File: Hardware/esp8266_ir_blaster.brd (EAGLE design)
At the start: 25.9 x 32.6 mm, 54 parts, among them Q1 600mA/40V, U1 ESP-12S, U2 38kHz, U3 3.3V

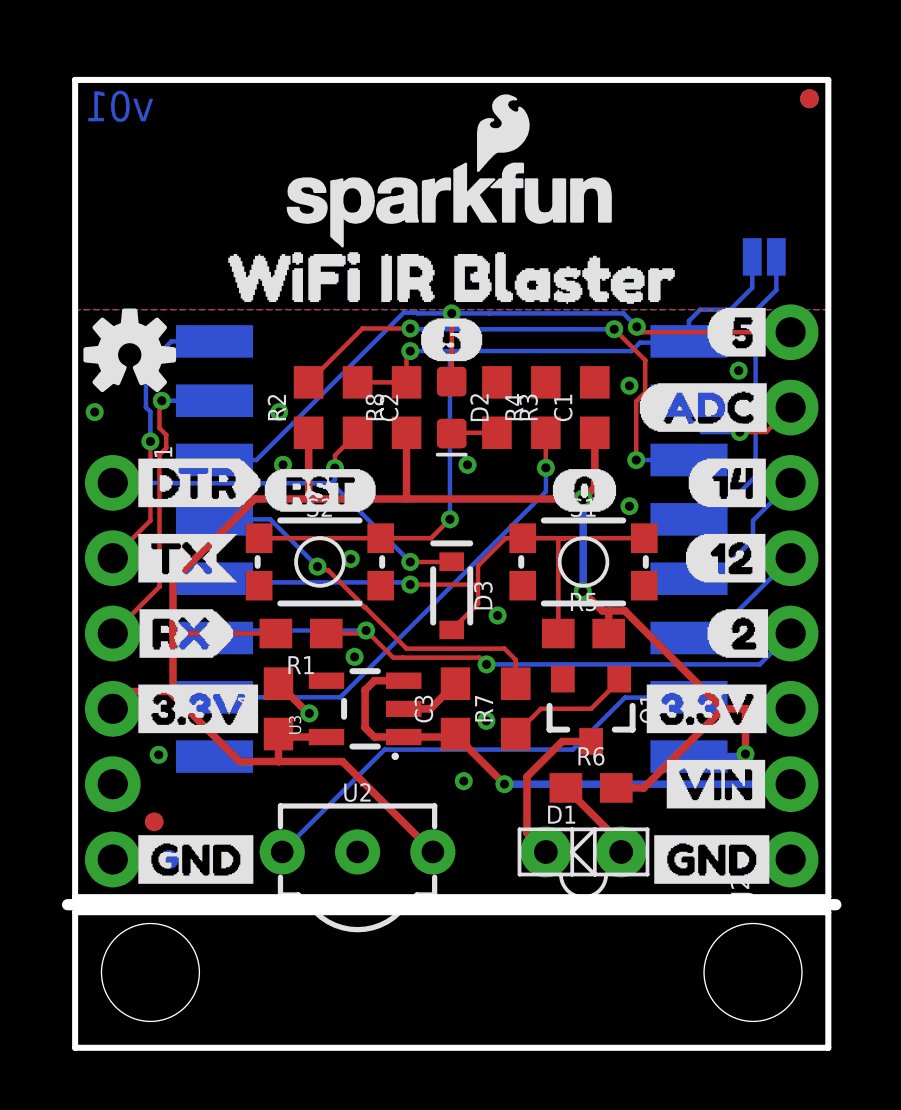
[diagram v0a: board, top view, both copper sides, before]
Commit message: Adding thermal pad
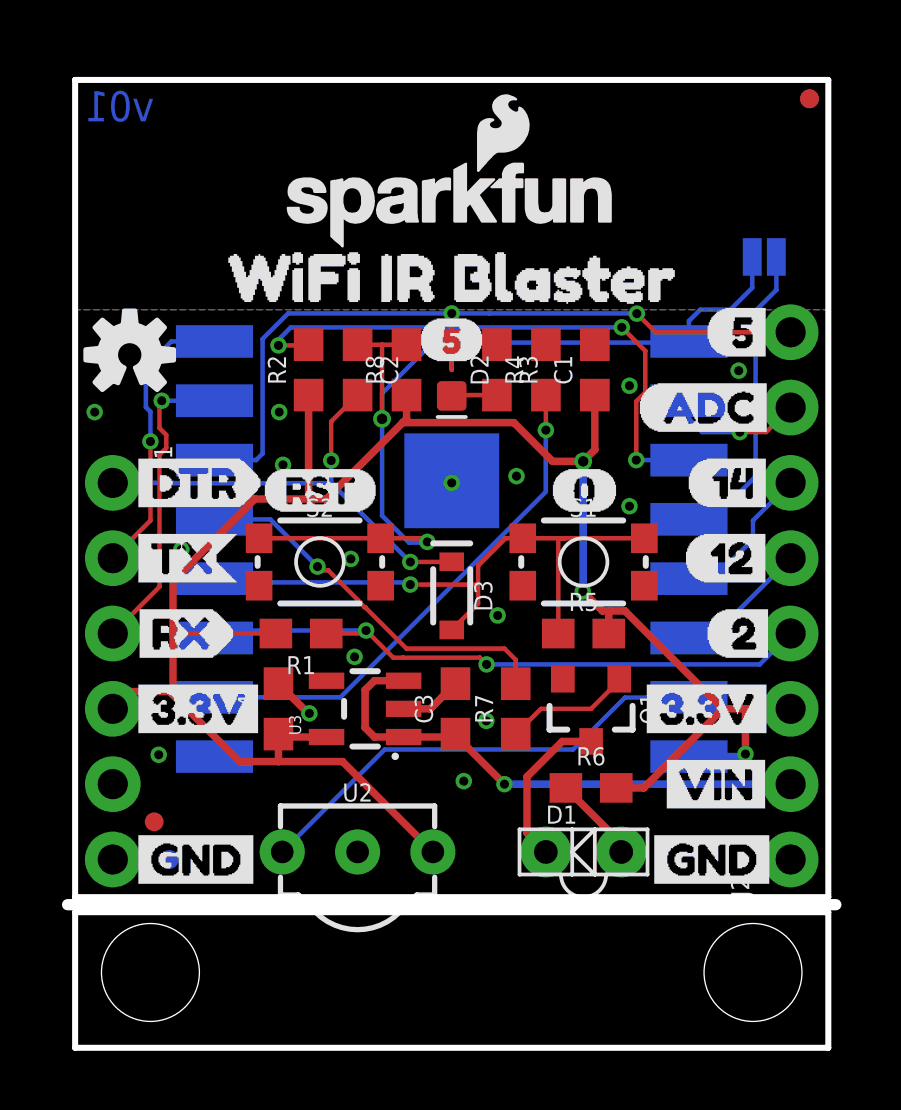
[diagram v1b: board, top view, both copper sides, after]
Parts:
- moved C1 1.27 mm to (17.5, 22.9)
- moved C2 1.27 mm to (9.53, 22.9)
- moved D2 1.27 mm to (12.7, 22.9)
- moved R2 1.27 mm to (7.87, 22.9)
- moved R3 1.27 mm to (14.2, 22.9)
- moved R4 1.27 mm to (15.9, 22.9)
- moved R8 1.27 mm to (11.2, 22.9)
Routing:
- net 3.3V: track 65.8 -> 68.6 mm
- net IO5: track 24.1 -> 26.8 mm
- net RESET: track 29.1 -> 31.3 mm
- net CHIP_EN: track 17.8 -> 19.7 mm
- net DTR: track 14.6 -> 16.0 mm
- net IO15: track 16.0 -> 17.3 mm
- net GND: vias 14 -> 16

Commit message: updating to reds
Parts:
- moved LOGO3 20.8 mm to (0.00, -27.9)
- moved FRAME1 20.8 mm to (-11.4, -25.4)
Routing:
- net GND: track 3.56 -> 6.16 mm, vias 16 -> 23
- net IO5: track 26.8 -> 25.1 mm
- net 3.3V: track 68.6 -> 67.8 mm
- net RESET: track 31.3 -> 32.1 mm
- net IO16: track 10.5 -> 11.1 mm
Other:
- board size 25.9 x 32.6 mm -> 25.9 x 33 mm

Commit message: post checklist changes
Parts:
- added U$7: (no value), buzzard_labels:NC0
- moved U$1 3.43 mm to (11.6, 20.4)
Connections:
- net GND: now also U1.P$1
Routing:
- net 3.3V: track 67.8 -> 68.3 mm
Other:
- board text added: "v10"
- board text removed: "v01"
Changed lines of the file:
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@@
 <wire x1="25.4" y1="33.02" x2="0" y2="33.02" width="0.2032" layer="20"/>
 <wire x1="0" y1="33.02" x2="0" y2="5.08" width="0.2032" layer="20"/>
-<text x="3.2385" y="31.4325" size="1.27" layer="16" font="vector" ratio="15" rot="MR0">v01</text>
+<text x="3.2385" y="31.4325" size="1.27" layer="16" font="vector" ratio="15" rot="MR0">v10</text>
 <text x="15.24" y="-25.4" size="1.778" layer="51" font="vector" ratio="15">Jim Lindblom</text>
 <wire x1="0" y1="4.572" x2="25.4" y2="4.572" width="0.2032" layer="20"/>
@@
 <attribute name="VALUE" x="14.224" y="25.019" size="0.6096" layer="27" font="vector" ratio="20" rot="R270" align="center"/>
 </element>
-<element name="U$1" library="buzzard_labels" package="512" value="" x="11.557" y="23.876" smashed="yes"/>
+<element name="U$1" library="buzzard_labels" package="512" value="" x="11.557" y="20.447" smashed="yes"/>
 <element name="J2" library="SparkFun-Connectors" package="1X08_NO_SILK" value="" x="24.13" y="6.35" smashed="yes" rot="R90">
 <attribute name="NAME" x="22.733" y="5.08" size="0.6096" layer="25" font="vector" ratio="20" rot="R90"/>
@@
 <element name="U$5" library="buzzard_labels-02" package="UART0" value="" x="1.27" y="20.828" rot="MR90"/>
 <element name="LOGO3" library="SparkFun-Aesthetics" package="REVISION" value="REVISION" x="0" y="-27.94"/>
+<element name="U$7" library="buzzard_labels" package="NC0" value="" x="1.651" y="8.89"/>
 </elements>
 <signals>
@@
 <wire x1="17.526" y1="23.71" x2="18.4785" y2="22.7575" width="0.254" layer="1"/>
 <via x="9.8044" y="18.5547" extent="1-16" drill="0.381"/>
+<contactref element="U1" pad="P$1"/>
 </signal>
 <signal name="3.3V">
@@
 <wire x1="6.858" y1="10.58" x2="6.858" y2="9.652" width="0.254" layer="1"/>
 <wire x1="1.27" y1="11.43" x2="1.2827" y2="11.4427" width="0.254" layer="1"/>
-<wire x1="3.7562875" y1="11.4427" x2="1.2827" y2="11.4427" width="0.254" layer="1"/>
+<wire x1="4.6355" y1="11.4427" x2="4.3912875" y2="11.4427" width="0.254" layer="1"/>
 <wire x1="20.7" y1="9.82" x2="22.52" y2="9.82" width="0.254" layer="16"/>
 <wire x1="22.52" y1="9.82" x2="22.606" y2="9.906" width="0.254" layer="16"/>
@@
 <wire x1="22.606" y1="9.906" x2="22.606" y2="11.43" width="0.254" layer="1"/>
 <contactref element="R5" pad="2"/>
-<wire x1="17.1196" y1="15.3924" x2="17.78" y2="14.732" width="0.254" layer="1"/>
-<wire x1="17.78" y1="14.732" x2="18.034" y2="14.732" width="0.254" layer="1"/>
-<wire x1="18.034" y1="14.732" x2="18.542" y2="14.732" width="0.254" layer="1"/>
-<wire x1="17.995" y1="13.97" x2="17.995" y2="14.693" width="0.254" layer="1"/>
-<wire x1="17.995" y1="14.693" x2="18.034" y2="14.732" width="0.254" layer="1"/>
 <wire x1="7.874" y1="22.01" x2="7.874" y2="18.5058" width="0.254" layer="1"/>
 <contactref element="J2" pad="3"/>
 <wire x1="24.13" y1="11.43" x2="22.606" y2="11.43" width="0.254" layer="1"/>
-<wire x1="21.844" y1="11.43" x2="22.606" y2="11.43" width="0.254" layer="1"/>
-<wire x1="18.542" y1="14.732" x2="21.844" y2="11.43" width="0.254" layer="1"/>
-<wire x1="18.249" y1="8.763" x2="19.177" y2="8.763" width="0.254" layer="1"/>
-<wire x1="19.177" y1="8.763" x2="21.844" y2="11.43" width="0.254" layer="1"/>
+<wire x1="18.249" y1="8.763" x2="19.05" y2="8.763" width="0.254" layer="1"/>
 <via x="17.1332" y="19.7758" extent="1-16" drill="0.381"/>
+<wire x1="19.05" y1="8.763" x2="19.177" y2="8.763" width="0.254" layer="1"/>
 <wire x1="17.1332" y1="19.7758" x2="17.1332" y2="15.406" width="0.254" layer="16"/>
 <wire x1="17.1332" y1="15.406" x2="17.1196" y2="15.3924" width="0.254" layer="16"/>
@@
 <wire x1="4.6355" y1="13.97" x2="4.6355" y2="17.2085" width="0.254" layer="1"/>
 <wire x1="6.77" y1="13.97" x2="4.6355" y2="13.97" width="0.254" layer="1"/>
-<wire x1="4.5085" y1="9.652" x2="3.7562875" y2="10.4042125" width="0.254" layer="1"/>
-<wire x1="3.7562875" y1="10.4042125" x2="3.7562875" y2="11.4427" width="0.254" layer="1"/>
-<wire x1="6.858" y1="9.652" x2="4.5085" y2="9.652" width="0.254" layer="1"/>
+<wire x1="5.3975" y1="9.652" x2="4.6452875" y2="10.4042125" width="0.254" layer="1"/>
+<wire x1="4.6452875" y1="10.4042125" x2="4.6452875" y2="11.4427" width="0.254" layer="1"/>
+<wire x1="6.858" y1="9.652" x2="5.3975" y2="9.652" width="0.254" layer="1"/>
 <wire x1="3.7562875" y1="11.4427" x2="3.7562875" y2="11.4427" width="0.254" layer="1"/>
-<wire x1="3.7562875" y1="11.4427" x2="3.7562875" y2="13.0907875" width="0.254" layer="1"/>
-<wire x1="3.7562875" y1="13.0907875" x2="4.6355" y2="13.97" width="0.254" layer="1"/>
+<wire x1="4.6355" y1="11.4427" x2="4.6355" y2="13.97" width="0.254" layer="1"/>
 <wire x1="11.176" y1="22.01" x2="11.176" y2="21.59" width="0.1778" layer="1"/>
+<wire x1="3.7562875" y1="11.4427" x2="1.2827" y2="11.4427" width="0.254" layer="1"/>
+<wire x1="4.6452875" y1="11.4427" x2="4.3912875" y2="11.4427" width="0.254" layer="1"/>
+<wire x1="4.3912875" y1="11.4427" x2="3.7562875" y2="11.4427" width="0.254" layer="1"/>
+<wire x1="19.05" y1="8.763" x2="19.685" y2="8.763" width="0.254" layer="1"/>
+<wire x1="19.685" y1="8.763" x2="20.066" y2="9.144" width="0.254" layer="1"/>
+<wire x1="20.066" y1="9.144" x2="20.066" y2="11.43" width="0.254" layer="1"/>
+<wire x1="20.066" y1="11.43" x2="20.066" y2="13.462" width="0.254" layer="1"/>
+<wire x1="20.066" y1="13.462" x2="19.558" y2="13.97" width="0.254" layer="1"/>
+<wire x1="19.558" y1="13.97" x2="17.995" y2="13.97" width="0.254" layer="1"/>
+<wire x1="17.995" y1="13.97" x2="17.995" y2="14.898" width="0.254" layer="1"/>
+<wire x1="17.5006" y1="15.3924" x2="17.1196" y2="15.3924" width="0.254" layer="1"/>
+<wire x1="17.995" y1="14.898" x2="17.5006" y2="15.3924" width="0.254" layer="1"/>
+<wire x1="22.606" y1="11.43" x2="20.066" y2="11.43" width="0.254" layer="1"/>
 </signal>
 <signal name="RXI">
@@
 <wire x1="11.3579" y1="16.0655" x2="8.636" y2="18.7874" width="0.1778" layer="16"/>
 <wire x1="8.636" y1="19.80541875" x2="8.636" y2="18.7874" width="0.1778" layer="16"/>
-<wire x1="9.525" y1="22.01" x2="8.636" y2="21.121" width="0.1778" layer="1"/>
-<wire x1="8.636" y1="21.121" x2="8.636" y2="19.80541875" width="0.1778" layer="1"/>
+<wire x1="9.525" y1="20.74" x2="8.636" y2="19.851" width="0.1778" layer="1"/>
+<wire x1="8.636" y1="19.851" x2="8.636" y2="19.80541875" width="0.1778" layer="1"/>
 <wire x1="12.7" y1="16.39" x2="12.199" y2="16.39" width="0.1778" layer="1"/>
 <wire x1="11.8745" y1="16.0655" x2="11.3665" y2="16.0655" width="0.1778" layer="1"/>
@@
 <wire x1="8.636" y1="18.7874" x2="1.5326" y2="18.7874" width="0.1778" layer="16"/>
 <wire x1="1.5326" y1="18.7874" x2="1.27" y2="19.05" width="0.1778" layer="16"/>
+<wire x1="9.525" y1="22.01" x2="9.525" y2="20.74" width="0.1778" layer="1"/>
 </signal>
 <signal name="CHIP_EN">
@@
 <wire x1="4.8881" y1="14.0081" x2="9.87555625" y2="14.0081" width="0.1778" layer="16"/>
 <via x="9.87555625" y="14.0081" extent="1-16" drill="0.381"/>
-<wire x1="9.87555625" y1="14.0081" x2="10.036828125" y2="13.846828125" width="0.1778" layer="1"/>
 <wire x1="8.47" y1="13.97" x2="9.83745625" y2="13.97" width="0.1778" layer="1"/>
 <wire x1="9.83745625" y1="13.97" x2="9.87555625" y2="14.0081" width="0.1778" layer="1"/>
